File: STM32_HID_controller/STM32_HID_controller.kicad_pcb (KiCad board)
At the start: 2 copper layers, 237.3 x 103.7 mm, 51 parts, among them J1 USB_B_Micro, J2 Conn_01x04_Pin, J3 Conn_01x03_Pin, J5 Conn_01x03_Pin, SW1 SW_SPDT, SW10 SW_Push, SW11 SW_Push, SW14 SW_Push, SW2 SW_Push, SW3 SW_Push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

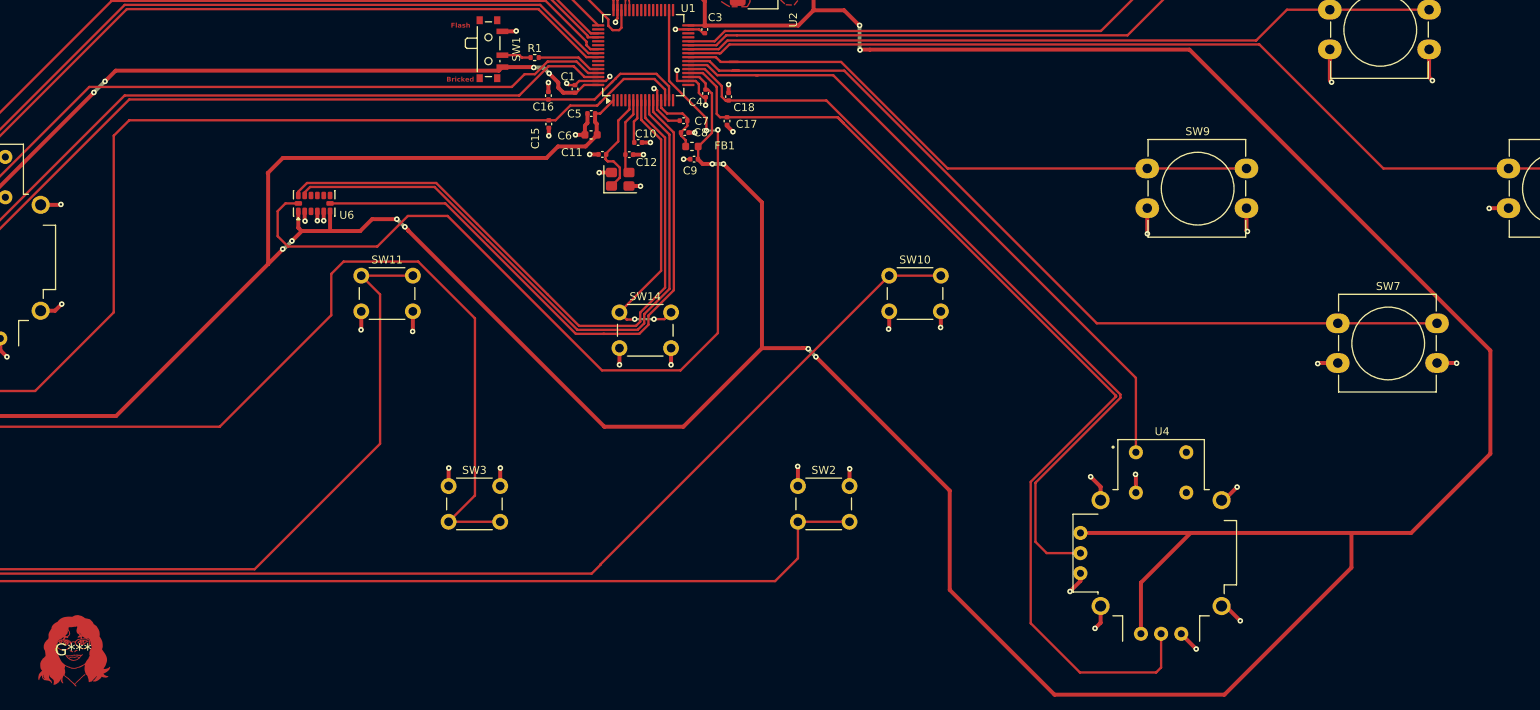
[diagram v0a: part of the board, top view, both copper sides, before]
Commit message: changed 3.3V routing
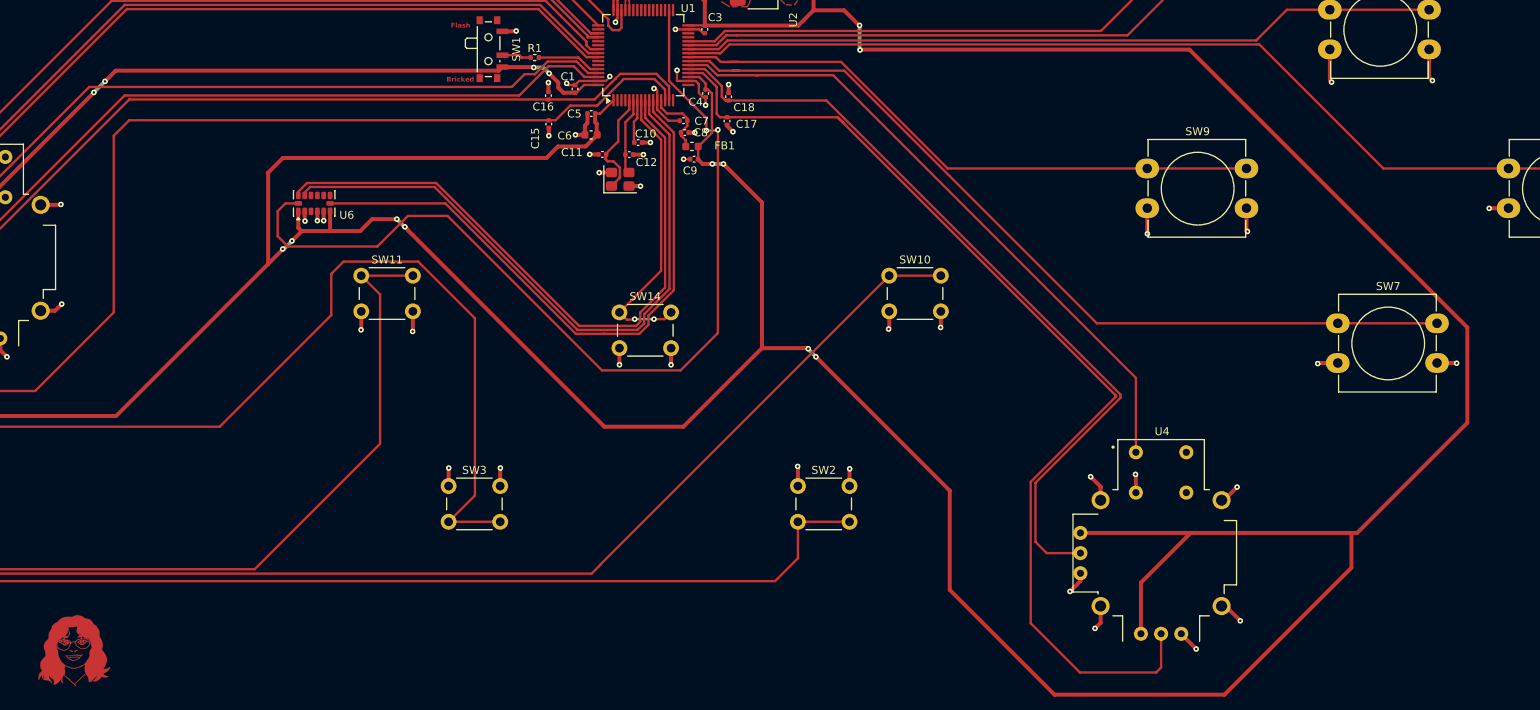
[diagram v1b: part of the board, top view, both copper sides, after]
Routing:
- net +3.3V: track 734.4 -> 728.0 mm
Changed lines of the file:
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@@
 			(at 0 0 0)
 			(layer "F.SilkS")
+			(hide yes)
 			(effects
 				(font
@@
 	)
 	(segment
+		(start 257.4 71.7)
+		(end 222.401 36.701)
+		(width 0.5)
+		(layer "F.Cu")
+		(net 2)
+	)
+	(segment
 		(start 146.15 41.15)
 		(end 145.17 42.13)
@@
 	)
 	(segment
+		(start 257.4 83.7)
+		(end 257.4 71.7)
+		(width 0.5)
+		(layer "F.Cu")
+		(net 2)
+	)
+	(segment
 		(start 135.855 38.9)
 		(end 135.406 39.349)
@@
 	)
 	(segment
+		(start 180.95 36.701)
+		(end 180.9 36.751)
+		(width 0.5)
+		(layer "F.Cu")
+		(net 2)
+	)
+	(segment
 		(start 173.7 74.3)
 		(end 174.3 74.3)
@@
 	)
 	(segment
-		(start 180.9 36.751)
-		(end 180.95 36.701)
-		(width 0.5)
-		(layer "F.Cu")
-		(net 2)
-	)
-	(segment
 		(start 158.65 84.2)
 		(end 148.7 84.2)
@@
 	)
 	(segment
+		(start 222.401 36.701)
+		(end 180.95 36.701)
+		(width 0.5)
+		(layer "F.Cu")
+		(net 2)
+	)
+	(segment
 		(start 56.3 65.05)
 		(end 56.3 64.75)
@@
 	)
 	(segment
-		(start 182.149 36.701)
-		(end 222.401 36.701)
-		(width 0.5)
-		(layer "F.Cu")
-		(net 2)
-	)
-	(segment
 		(start 56.3 70.4)
 		(end 56.4 70.4)
@@
 	)
 	(segment
+		(start 243.52 97.58)
+		(end 257.4 83.7)
+		(width 0.5)
+		(layer "F.Cu")
+		(net 2)
+	)
+	(segment
 		(start 68.85 82.85)
 		(end 87.2 82.85)
@@
 	)
 	(segment
-		(start 260.3 74.6)
-		(end 260.3 87.6)
-		(width 0.5)
-		(layer "F.Cu")
-		(net 2)
-	)
-	(segment
 		(start 141.4 50.35)
 		(end 142.85 48.9)
@@
 	)
 	(segment
-		(start 250.32 97.58)
-		(end 242.8 97.58)
-		(width 0.5)
-		(layer "F.Cu")
-		(net 2)
-	)
-	(segment
 		(start 178.9 31.75)
 		(end 180.8 33.65)
@@
 	)
 	(segment
-		(start 260.3 87.6)
-		(end 250.32 97.58)
-		(width 0.5)
-		(layer "F.Cu")
-		(net 2)
-	)
-	(segment
 		(start 147.53 45.83)
 		(end 147.735 46.035)
@@
 	)
 	(segment
-		(start 180.95 36.701)
-		(end 182.149 36.701)
-		(width 0.5)
-		(layer "F.Cu")
-		(net 2)
-	)
-	(segment
 		(start 135.406 39.349)
 		(end 87.151 39.349)
@@
 	)
 	(segment
+		(start 242.8 97.58)
+		(end 243.52 97.58)
+		(width 0.5)
+		(layer "F.Cu")
+		(net 2)
+	)
+	(segment
 		(start 124 59.45)
 		(end 123.569975 59.019975)
@@
 		(width 0.5)
 		(layer "F.Cu")
-		(net 2)
-	)
-	(segment
-		(start 222.401 36.701)
-		(end 260.3 74.6)
-		(width 0.5)
-		(layer "F.Cu")

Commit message: added mpu to everything, final draft before review
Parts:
- added C19: .1u, Capacitor_SMD:C_0402_1005Metric, F.Cu at (98.9, 52.5)
- added C20: .1u, Capacitor_SMD:C_0402_1005Metric, F.Cu at (97.6, 60.4)
- added R3: 4.7k, Resistor_SMD:R_0402_1005Metric, F.Cu at (94.1, 52.5)
- added R4: 4.7k, Resistor_SMD:R_0402_1005Metric, F.Cu at (96.5, 52.5)
- added U7: MPU-6050, Sensor_Motion:InvenSense_QFN-24_4x4mm_P0.5mm, F.Cu at (96.0, 56.4)
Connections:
- U1 pad 29: unconnected-(U1-PB10-Pad29) -> i2c_scl
- U1 pad 53: unconnected-(U1-PC12-Pad53) -> i2c_sda
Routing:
- net i2c_scl: track 0.00 -> 72.7 mm, vias 0 -> 4
- net i2c_sda: track 0.00 -> 64.9 mm, vias 0 -> 4
- net +3.3V: track 728.0 -> 771.6 mm
- net GND: track 144.9 -> 153.4 mm, vias 66 -> 71
- net Net-(U7-CPOUT): track 0.00 -> 2.77 mm
- net Net-(U7-REGOUT): track 0.00 -> 2.38 mm
